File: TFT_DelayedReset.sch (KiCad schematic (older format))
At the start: 10 parts, among them U4 MIC1555-YM5, U6 MCP1415

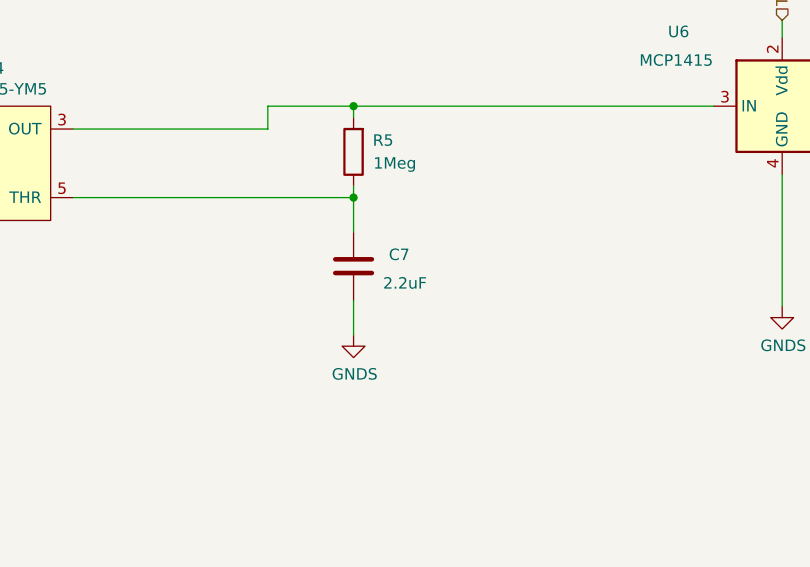
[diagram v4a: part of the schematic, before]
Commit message: updates
set U3 4051 address resistors to E12 values
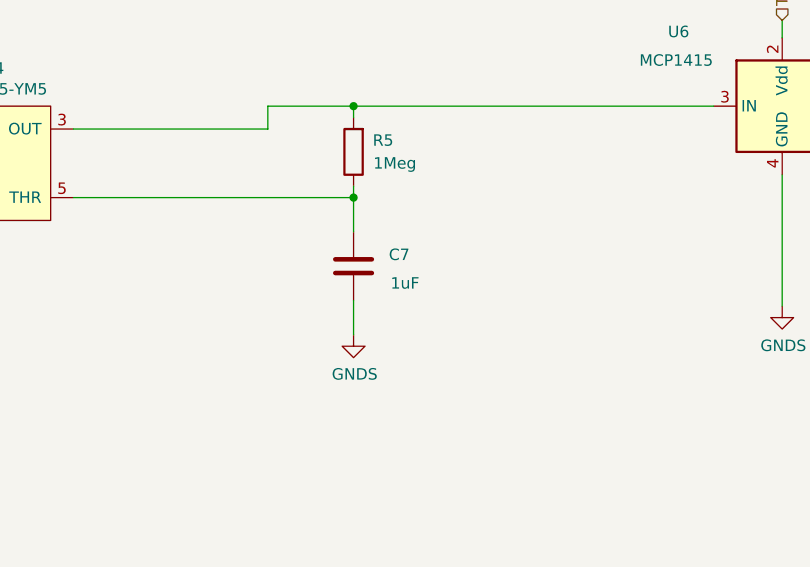
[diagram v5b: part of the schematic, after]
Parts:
- C7: value 2.2uF -> 1uF
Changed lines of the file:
@@
 AR Path="/5F02F4E9/5F1755C4/5F127B66" Ref="C7"  Part="1"
 F 0 "C7" H 5275 2800 50  0000 C CNN
-F 1 "2.2uF" H 5250 2925 50  0000 C CNN
+F 1 "1uF" H 5250 2925 50  0000 C CNN
 F 2 "Capacitor_SMD:C_0805_2012Metric_Pad1.15x1.40mm_HandSolder" H 5513 2700 50  0001 C CNN
 F 3 "~" H 5475 2850 50  0001 C CNN
